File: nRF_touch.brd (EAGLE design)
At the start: 46.4 x 79.5 mm, 46 parts, among them Q1 BSS138BKW, T1 BSS84, T2 BC847/2N7002, U1 ADP160, U2 AT42QT1010-TSHR

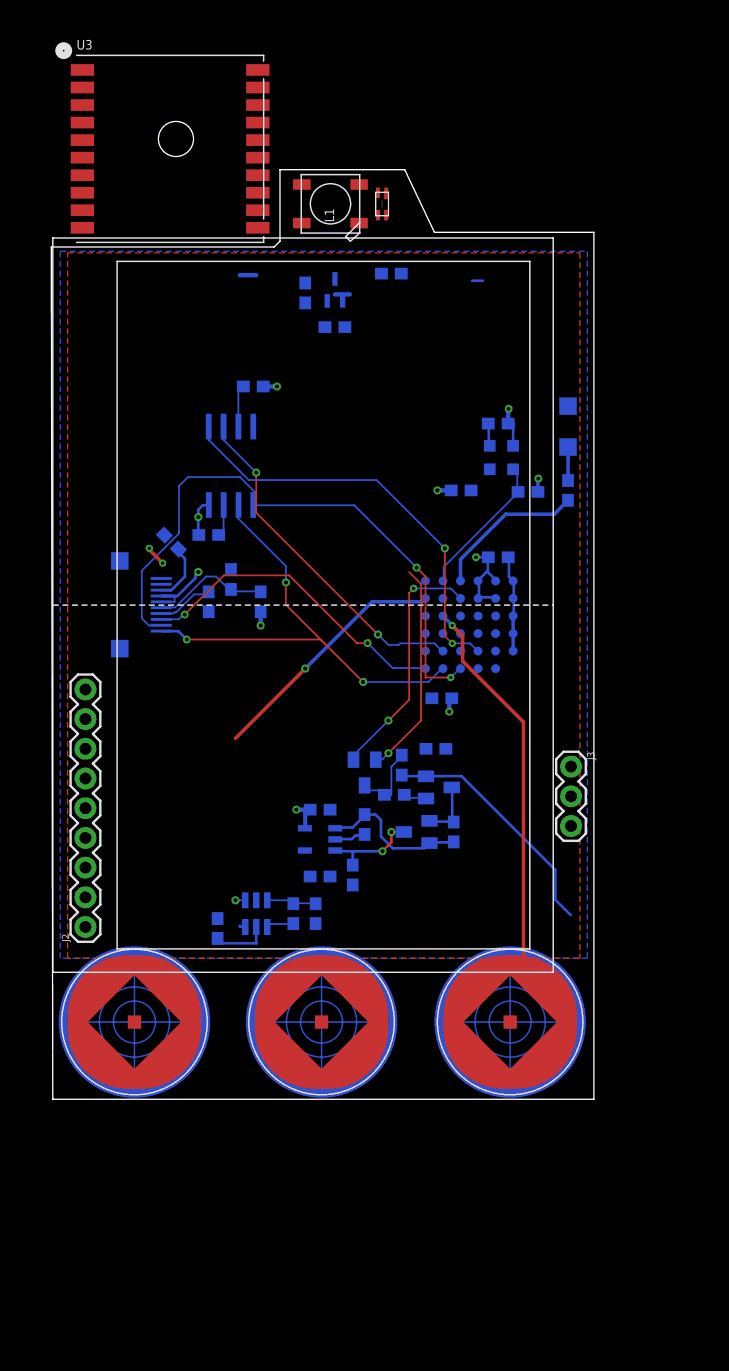
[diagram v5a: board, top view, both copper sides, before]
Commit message: Start placing components
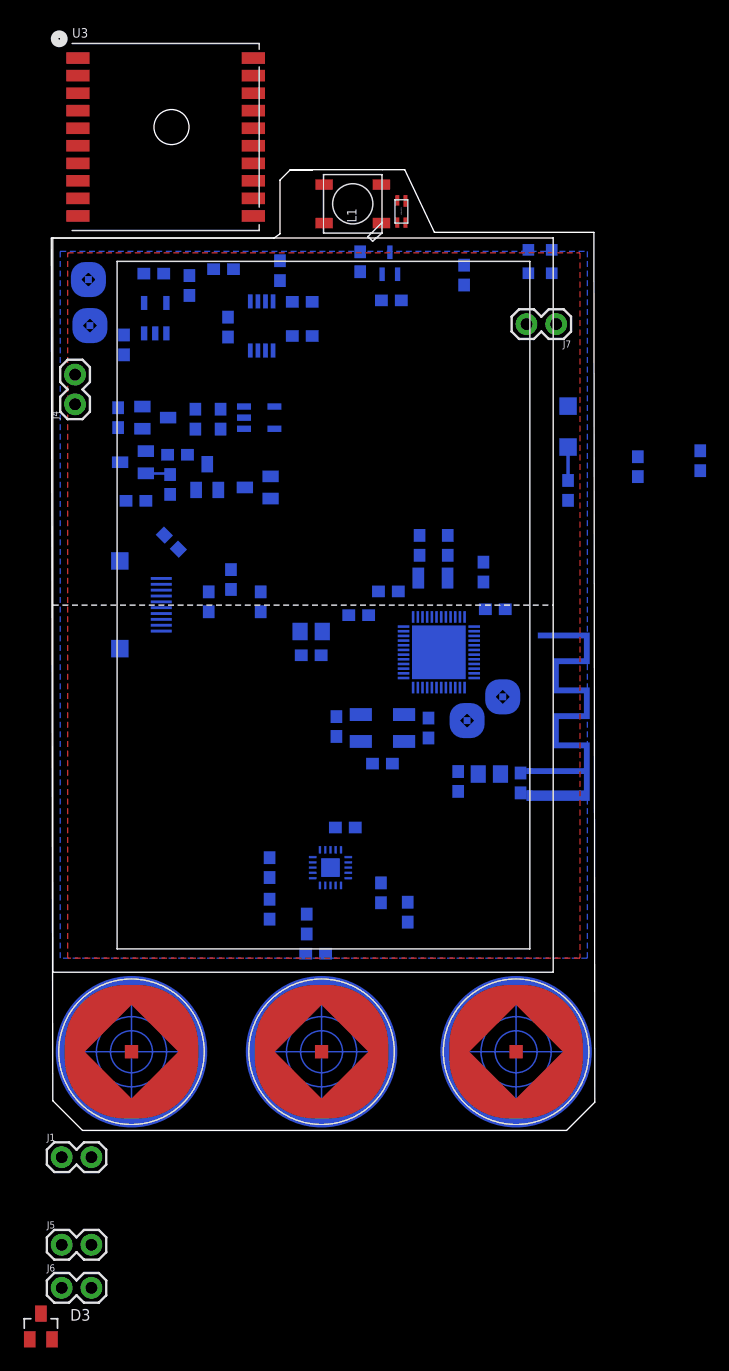
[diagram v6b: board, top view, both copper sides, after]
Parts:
- removed J2: (no value), SparkFun-Connectors:1X09
- removed J3: (no value), SparkFun-Connectors:1X03
- removed R3, R4: 4.7k, SparkFun-Resistors:0603
- removed U$1: N5150, N5:N5150
- added C12, C17: 4.7uF, SparkFun-Capacitors:0603
- added C13, C14, C16, C18, C19: 0.1uF, SparkFun-Capacitors:0603
- added C15: 1uF, SparkFun-Capacitors:0603
- added C20, C21, C22, C23: 12pF, SparkFun-Capacitors:0603
- added C24: 100pF, SparkFun-Capacitors:0603
- added C25: 0.8pF, SparkFun-Capacitors:0603
- added C26: DNP, SparkFun-Capacitors:0603
- added D2: BAT54C, nxp_60:SOT23
- added D3: BAT754A, nxp_60:SOT23
- added E1: ANTENNA-GROUNDEDTRACE-15.2MM, SparkFun-RF:TRACE_ANTENNA_2.4GHZ_15.2MM
- added FB1: FB_0805, ferrite_beads:L0805
- added FB2: 3.9nH, ferrite_beads:L0805
- added IC1: MCP73831/OT, adafruit:SOT23-5L
- added J1, J4, J5, J6, J7: (no value), SparkFun-Connectors:1X02
- added MBAT, SWDCLK, SWDIO, VBAT: TESTPOINT, test_points:TESTPOINT
- added R16, R17: 10k, SparkFun-Resistors:0603
- added R18: 2k, SparkFun-Resistors:0603
- added R19: 0.010, SparkFun-Resistors:0603
- added U$6: NRF52832NRF52832-QFAA, NRF52832:QFN48
- added Y1: 32.768kHz, SparkFun-Clocks:CRYSTAL-SMD-3.2X1.5MM
- added Y2: 32MHz-3.2X2.5, SparkFun-Clocks:CRYSTAL-SMD-5X3.2-4PAD
- C2, C4: value 0.1uF -> 22nF
- C5: value 1uF -> 220nF
- R1: value 4.7k -> 200k
- R2: value 4.7k -> 1k
- U$3: value FLASH -> STC3100; device FlashMem:SOIC8 -> STC3100:STC3100
- U2: value AT42QT1010-TSHR -> AT42QT1040; device AT42QT1010:SOT95P280X145-6N -> AT42QT1040:VQFN20
- moved C6 48.0 mm to (8.64, 70.6)
- moved C8 45.9 mm to (6.10, 64.5)
- moved C4 45.8 mm to (21.7, 15.0), turned to 270 degrees
- moved R8 45.6 mm to (5.59, 58.3), turned to 90 degrees
- moved T1 41.9 mm to (8.76, 58.3), turned to 90 degrees
- moved C9 41.2 mm to (12.2, 58.2), turned to 90 degrees
- moved R13 40.0 mm to (14.4, 58.2), turned to 270 degrees
- moved T2 38.2 mm to (6.86, 54.5), turned to 270 degrees
- moved U1 36.4 mm to (17.7, 58.3), turned to 90 degrees
- moved C5 35.9 mm to (21.3, 68.2)
- moved R9 34.5 mm to (10.7, 55.1), turned to 0 degrees
- moved C11 33.3 mm to (7.11, 51.2), turned to 0 degrees
- moved R10 31.1 mm to (10.0, 52.6), turned to 90 degrees
- moved C2 30.4 mm to (28.1, 17.7), turned to 90 degrees
- moved D1 28.6 mm to (13.2, 53.2), turned to 0 degrees
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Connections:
- removed net 5V: C10.2, C8.1, J2.1, R8.2, T1.2, U1.1, U2.5
- removed net AIN3: S3.P$1, U$1.F5
- removed net AIN5: S1.P$1, U$1.E4
- removed net AT42_OUT: D1.2, U2.1
- removed net N$1: R12.2, U$1.D6
- removed net PAD: R11.1, S2.P$1
- removed net SPIS_MI: J2.5
- removed net SPIS_MO: J2.6
- removed net SPIS_SCK: J2.4
- removed net SST_CS: J2.7, U$3.CE
- new net AT42_COUT: D1.2, U$6.21, U2.P14
- new net AT42_DOUT: U$6.20, U2.P13
- new net AT42_GOUT: U$6.22, U2.P11
- new net CHRG_END: IC1.1, U$6.23
- new net CPAD: R17.1, S2.P$1
- new net DPAD: R16.1, S1.P$1
- new net GPAD: R11.1, S3.P$1
- new net LED_PIN: R12.2, U$6.17
- new net MBAT: MBAT.P$1, R19.1, U$3.CG
- new net N$14: IC1.5, R18.2
- new net N$16: R1.1, U$3.ROSC
- new net N$17: C15.1, FB1.2, U$6.46
- new net N$18: C25.1, FB2.2, U$6.30
- new net N$19: FB1.1, U$6.47
- new net N$20: C16.1, U$6.1
- new net N$21: C26.1, E1.ANT, FB2.1
- new net N$24: C20.2, U$6.2, Y1.P$2
- new net N$25: C21.2, U$6.3, Y1.P$1
- new net N$27: C22.1, U$6.35, Y2.1
- new net N$28: C23.1, U$6.34, Y2.3
- new net N$3: C2.2, R16.2, U2.P15
- new net N$4: C2.1, U2.P16
- new net N$5: C4.2, R17.2, U2.P20
- new net N$9: C4.1, U2.P1
- new net SELF_EN: D2.2, U$6.18
- new net VBAT: C10.2, C8.1, IC1.3, R8.2, T1.2, U1.1, U2.P9, VBAT.P$1
- new net VUSB: C6.1, D2.1, IC1.4, J4.2
- net 5150_CS: now also J4.1, U$6.40; no longer J2.3, U$1.D2
- net GND: now also C12.1, C13.1, C14.1, C15.2, C16.2, C17.1, C18.2, C19.2, C20.1, C21.1, C22.2, C23.2, C24.2, C25.2, C26.2, C5.1, E1.GND, IC1.2, J1.1, R1.2, R18.1, R19.2, U$3.GND, U$6.31, U$6.45, U$6.GND, U2.GND, U2.P8, Y2.2, Y2.4; no longer C2.2, C4.2, C5.2, J2.2, U$1.A2, U$1.A3, U$1.A4, U$1.A5, U$1.A6, U$3.VSS, U2.2, U2.6
- net N$12: now also C5.2, R2.1, U$3.VIN; no longer R1.2, U$3.WP
- net N$15: now also C24.1, U$6.33; no longer R2.1, U$3.HOLD
- net N$6: now also U2.P4; no longer U2.3
- net N$7: now also U2.P5; no longer U2.4
- net NEO_PIN: now also U$6.19; no longer U$1.F1
- net NRF_EN: now also D2.3; no longer U$1.D5
- net SCL: now also J7.2, U$3.SCL; no longer R4.2, U$1.F6
- net SDA: now also J7.1, U$3.SDA; no longer R3.1, U$1.E6
- net SHARP_CS: now also J5.2, U$6.41
- net SPIM_DIN: now also J6.2, U$6.38; no longer U$1.E2, U$3.SO
- net SPIM_DO: now also J5.1, U$6.39; no longer U$1.D1, U$3.SI
- net SPIM_SCK: now also J6.1, U$6.37; no longer U$1.E1, U$3.SCK
- net SWDCLK: now also SWDCLK.P$1, U$6.25; no longer J3.2, U$1.C1
- net SWDIO: now also SWDIO.P$1, U$6.26; no longer J3.1, U$1.B1
- net SW_POWER: now also C3.1, R2.2, U$3.VCC
- net VCC: now also C12.2, C13.2, C14.2, C17.2, C18.1, C19.1, J1.2, U$6.13, U$6.36, U$6.48; no longer C2.1, C3.1, C4.1, C5.1, C6.1, J2.9, J3.3, R1.1, R2.2, R3.2, R4.1, U$1.B5, U$1.B6, U$1.C5, U$1.C6, U$3.VDD
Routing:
- net SPIM_DO: track 52.3 -> 0.00 mm, vias 2 -> 0
- net SPIM_SCK: track 41.0 -> 0.00 mm, vias 3 -> 0
- net GND: track 40.0 -> 2.15 mm, vias 2 -> 0
- net SST_CS: track 36.0 -> 0.00 mm, vias 2 -> 0
- net AIN5: track 33.9 -> 0.00 mm, vias 1 -> 0
- net VCC: track 32.8 -> 0.09 mm, vias 10 -> 0
- net SPIM_DIN: track 29.5 -> 0.00 mm, vias 2 -> 0
- net SHARP_CS: track 27.4 -> 0.00 mm, vias 2 -> 0
- net AIN3: track 21.2 -> 0.00 mm, vias 1 -> 0
- net NRF_EN: track 21.2 -> 0.00 mm, vias 2 -> 0
- net AT42_OUT: track 19.2 -> 0.00 mm, vias 2 -> 0
- net 5V: track 17.9 -> 0.00 mm
- net N$1: track 13.1 -> 0.00 mm
- net SDA: track 13.0 -> 0.00 mm
- net DISP: track 10.3 -> 0.18 mm
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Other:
- board size 46.4 x 79.5 mm -> 46.5 x 82.2 mm

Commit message: Finished placing
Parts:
- removed D1: BAT54C, nxp_60:SOT23
- added C27, C28: 4.7uF, SparkFun-Capacitors:0603
- added C29: 0.1uF, SparkFun-Capacitors:0603
- added R3: 47, SparkFun-Resistors:0603
- added R4: 80, SparkFun-Resistors:0603
- added T3, T4: BC847, nxp_60:SOT23
- added U$1, U$7, U$8: KPA-2106SECK, KPA_LED:KPA-2106SECK
- D3: value BAT754A -> BAT54A
- MBAT, SWDCLK, SWDIO, VBAT: value TESTPOINT -> TESTPOINT_22; device test_points:TESTPOINT -> test_points:TESTPOINT_22
- T2: value BC847/2N7002 -> BC847
- moved D3 70.9 mm to (6.60, 51.1), flipped to the bottom
- moved J5 36.8 mm to (3.05, 24.3), turned to 90 degrees
- moved J1 36.1 mm to (3.05, 31.1), turned to 90 degrees
- moved J6 34.0 mm to (3.05, 17.8), turned to 90 degrees
- moved C14 28.2 mm to (22.7, 61.3), turned to 180 degrees
- moved C13 20.1 mm to (44.7, 71.6), turned to 90 degrees
- moved MBAT 11.7 mm to (14.6, 68.1)
- moved U$2 9.54 mm to (19.9, 75.4)
- moved T2 8.32 mm to (15.1, 53.5), turned to 90 degrees
- moved U1 7.67 mm to (10.4, 60.8), turned to 180 degrees
- moved D2 7.22 mm to (14.6, 58.9), turned to 0 degrees
- moved R7 5.76 mm to (12.2, 43.9), turned to 270 degrees
- moved C8 5.64 mm to (3.17, 69.3), turned to 90 degrees
- moved FB1 4.20 mm to (26.3, 39.8)
- moved R9 3.45 mm to (11.7, 51.8), turned to 270 degrees
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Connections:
- removed net NRF_EN: D1.1, D2.3
- new net LED_BCK: T3.1, T4.1, U$6.16
- new net N$1: R9.2, T2.1
- new net N$10: R3.2, U$1.P$2, U$7.P$2
- new net N$22: T4.3, U$8.P$1
- new net SW_AT: C9.1, D2.2, L1.1-VDD, R13.2, R14.2, T1.3
- new net TRANS: D3.1, T2.3
- net AT42_COUT: now also D3.2, U2.P12; no longer D1.2, U2.P14
- net CHRG_END: now also U$6.43; no longer U$6.23
- net GND: now also C27.1, C28.1, C29.1, T3.2, T4.2
- net N$11: now also R4.2, U$8.P$2; no longer C11.1, R9.2, T2.1
- net N$13: now also T3.3, U$1.P$1, U$7.P$1; no longer D1.3, R10.1, R9.1
- net N$5: now also U2.P2; no longer U2.P20
- net N$8: now also C11.1, D3.3; no longer T2.3
- net N$9: now also U2.P3; no longer U2.P1
- net SCL: now also U$6.23
- net SDA: now also U$6.18
- net SELF_EN: now also R10.1, R9.1, U$6.42; no longer D2.2, U$6.18
- net SW_POWER: now also D2.3; no longer C9.1, L1.1-VDD, R13.2, R14.2, T1.3
- net VBAT: now also C28.2
- net VCC: now also C27.2, C29.2, R3.1, R4.1
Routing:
- net N$18: track 0.00 -> 9.59 mm
- net N$21: track 0.00 -> 2.59 mm
- net GND: track 2.15 -> 0.00 mm
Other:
- outline, holes or cut-outs redrawn

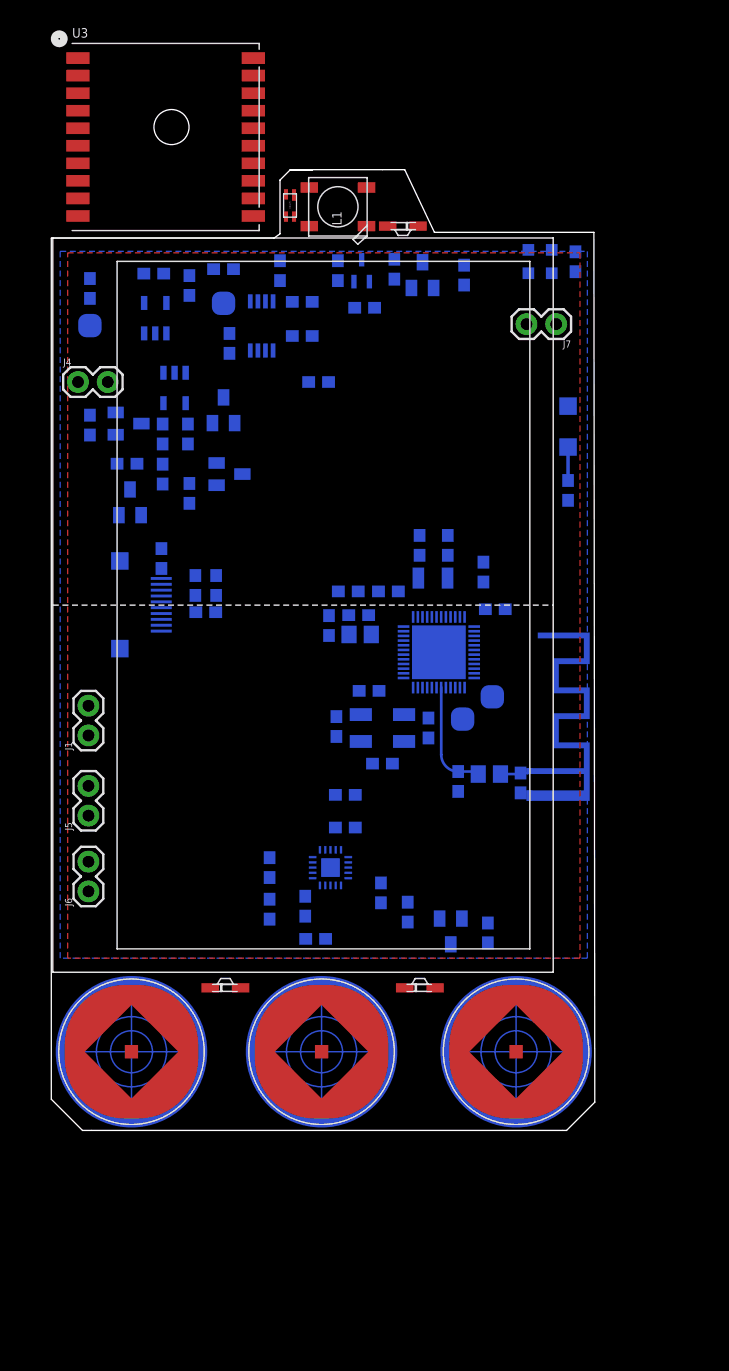
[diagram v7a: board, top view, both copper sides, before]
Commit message: First try at routing
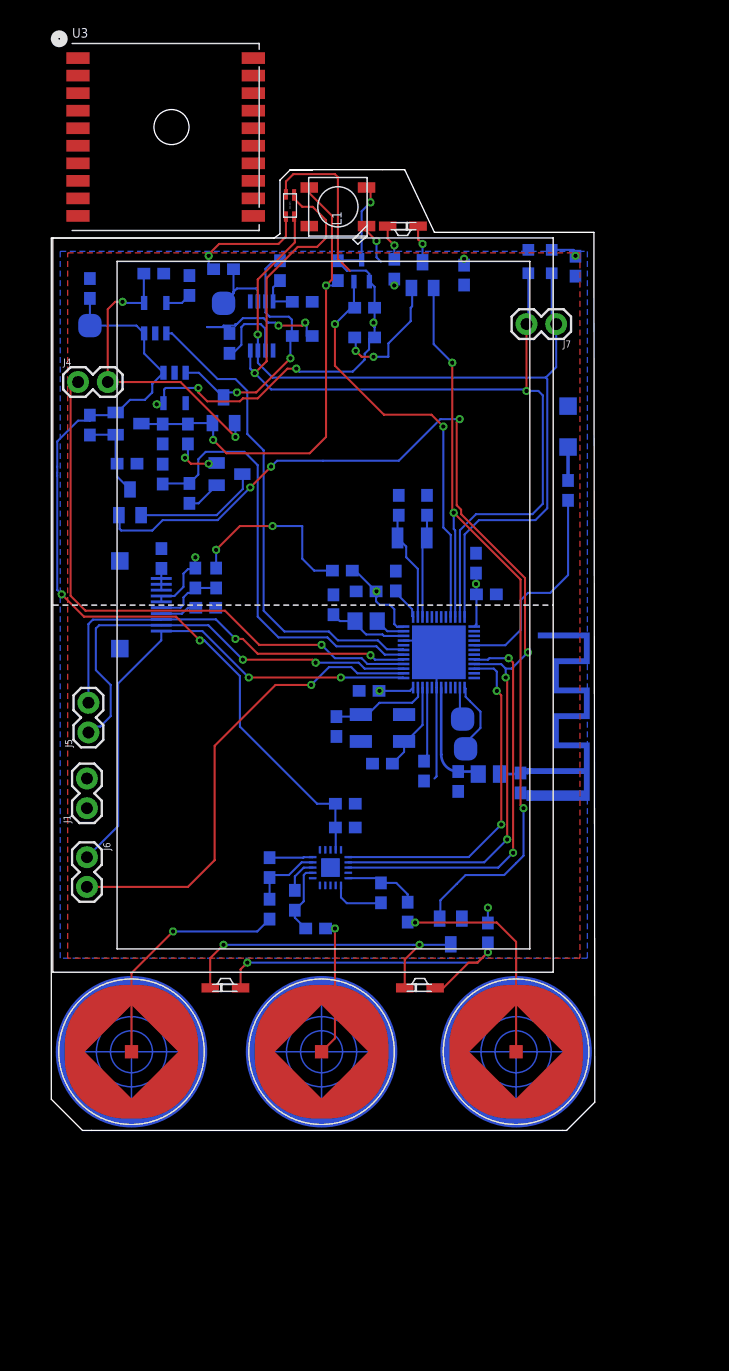
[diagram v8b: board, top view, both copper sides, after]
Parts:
- moved J5 7.11 mm to (3.05, 31.4)
- moved J1 6.22 mm to (2.92, 24.9)
- moved C14 5.48 mm to (26.7, 65.2)
- moved SWDCLK 5.00 mm to (35.3, 30.0)
- moved Y1 3.86 mm to (30.7, 48.0)
- moved C20 3.86 mm to (29.6, 50.8)
- moved C21 3.86 mm to (32.0, 50.8)
- moved C24 3.70 mm to (31.8, 28.1)
- moved J6 2.92 mm to (2.92, 20.7), turned to 270 degrees
- moved C18 2.13 mm to (26.8, 43.4)
- moved C27 1.85 mm to (24.8, 45.2)
- moved C15 1.82 mm to (24.0, 42.3)
- moved C17 1.48 mm to (37.1, 43.2)
- moved FB1 1.25 mm to (26.8, 40.9)
- moved C16 1.09 mm to (29.3, 44.3), turned to 90 degrees
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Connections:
- new net N$31: U$6.8
- net LED_BCK: now also U$6.10; no longer U$6.16
- net NEO_PIN: now also U$6.9; no longer U$6.19
- net SCL: now also U$6.11; no longer U$6.23
- net SDA: now also U$6.12; no longer U$6.18
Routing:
- net AT42_COUT: track 0.00 -> 91.3 mm, vias 0 -> 6
- net SCL: track 0.00 -> 83.1 mm, vias 0 -> 2
- net SDA: track 0.00 -> 74.7 mm, vias 0 -> 1
- net GND: track 0.00 -> 74.7 mm, vias 0 -> 10
- net VCC: track 0.00 -> 74.4 mm, vias 0 -> 12
- net VBAT: track 0.08 -> 74.1 mm, vias 0 -> 2
- net LED_BCK: track 0.00 -> 71.0 mm, vias 0 -> 3
- net 5150_CS: track 0.00 -> 49.4 mm, vias 0 -> 1
- net SPIM_SCK: track 0.00 -> 44.4 mm, vias 0 -> 2
- net SW_AT: track 0.00 -> 41.8 mm, vias 0 -> 2
- net CHRG_END: track 0.00 -> 41.7 mm
- net SPIM_DIN: track 0.00 -> 40.8 mm, vias 0 -> 1
- net SPIM_DO: track 0.00 -> 38.5 mm, vias 0 -> 2
- net SELF_EN: track 0.00 -> 37.3 mm
- net NEO_PIN: track 0.00 -> 36.1 mm, vias 0 -> 2
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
